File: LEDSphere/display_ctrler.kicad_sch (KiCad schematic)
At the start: 38 parts, among them J101 CONN_01x02, J301 USB_C_Receptacle_USB2.0, J302 Micro_SD_Card, U1 SN74AHC1G14DBVR, U101 W25Q128JVP, U301 USBLC6-2SC6, U303 RP2040, U305 ESP01s, Y301 12MHz

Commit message: finish display controller layout
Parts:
- J301: footprint project_lib:CUI_UJ20-C-V-C-1-SMT-TR -> Footprints:CUI_UJ20-C-V-C-1-SMT-TR
- J302: footprint project_lib:CUI_MSD-4-A -> Footprints:CUI_MSD-4-A
- U305: footprint project_lib:ESP01s_SMD -> Footprints:ESP01s_SMD
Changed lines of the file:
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@@
 			)
 		)
-		(property "Footprint" "project_lib:CUI_UJ20-C-V-C-1-SMT-TR"
+		(property "Footprint" "Footprints:CUI_UJ20-C-V-C-1-SMT-TR"
 			(at 33.02 53.34 0)
 			(hide yes)
@@
 			)
 		)
-		(property "Footprint" "project_lib:ESP01s_SMD"
+		(property "Footprint" "Footprints:ESP01s_SMD"
 			(at 246.38 71.12 0)
 			(hide yes)
@@
 			)
 		)
-		(property "Footprint" "project_lib:CUI_MSD-4-A"
+		(property "Footprint" "Footprints:CUI_MSD-4-A"
 			(at 13.97 156.21 0)
 			(show_name no)

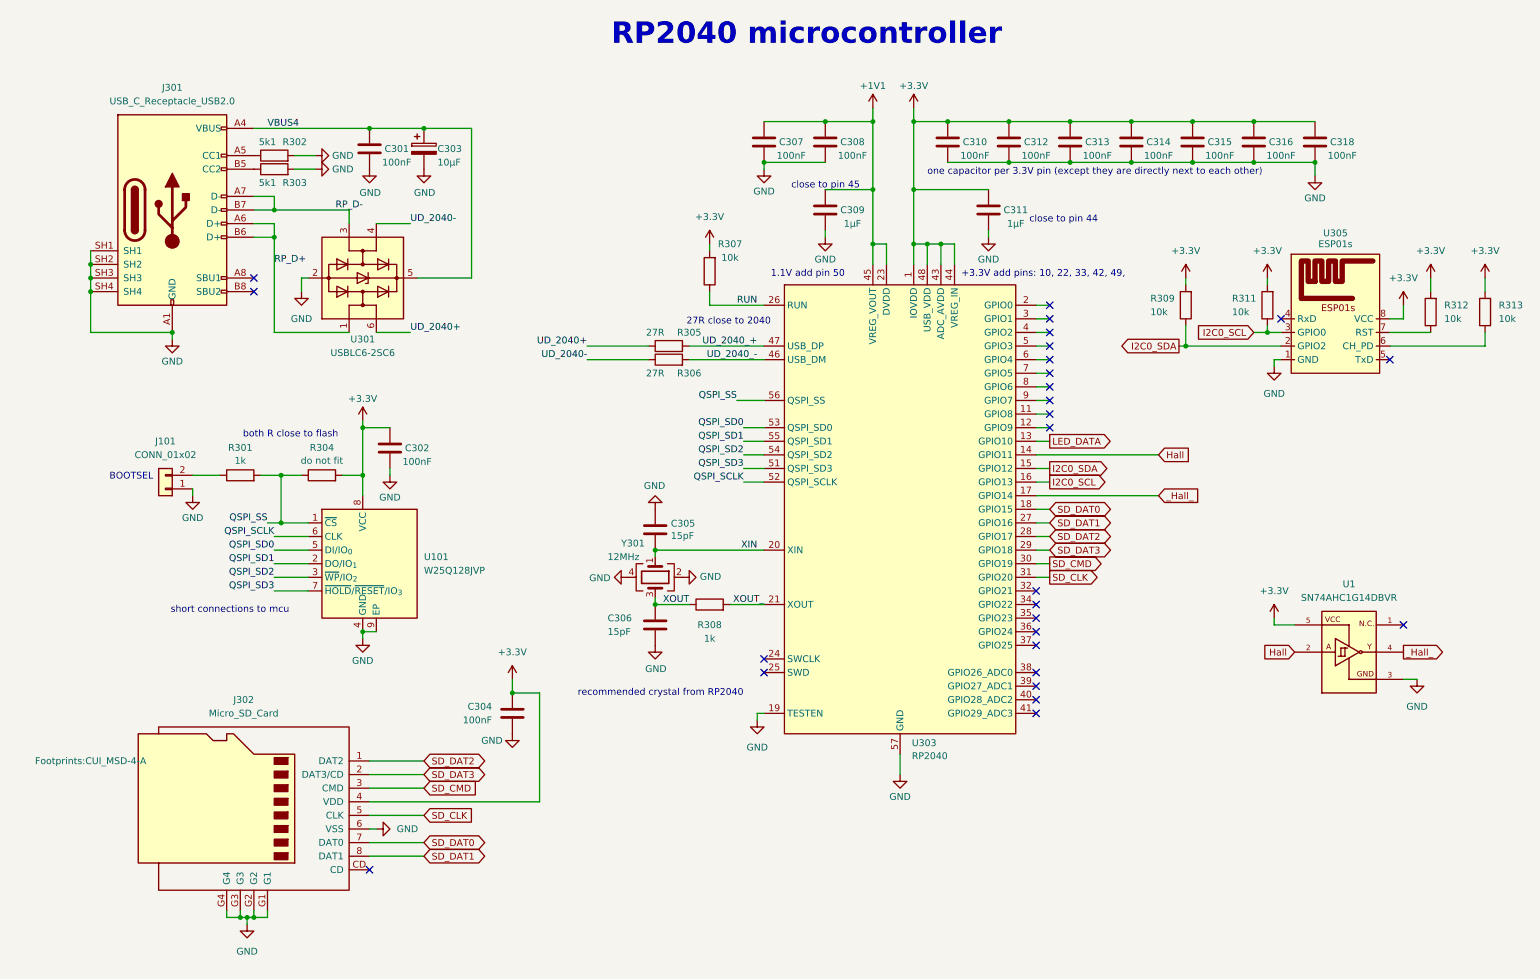
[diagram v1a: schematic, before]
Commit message: display controller add led terminal
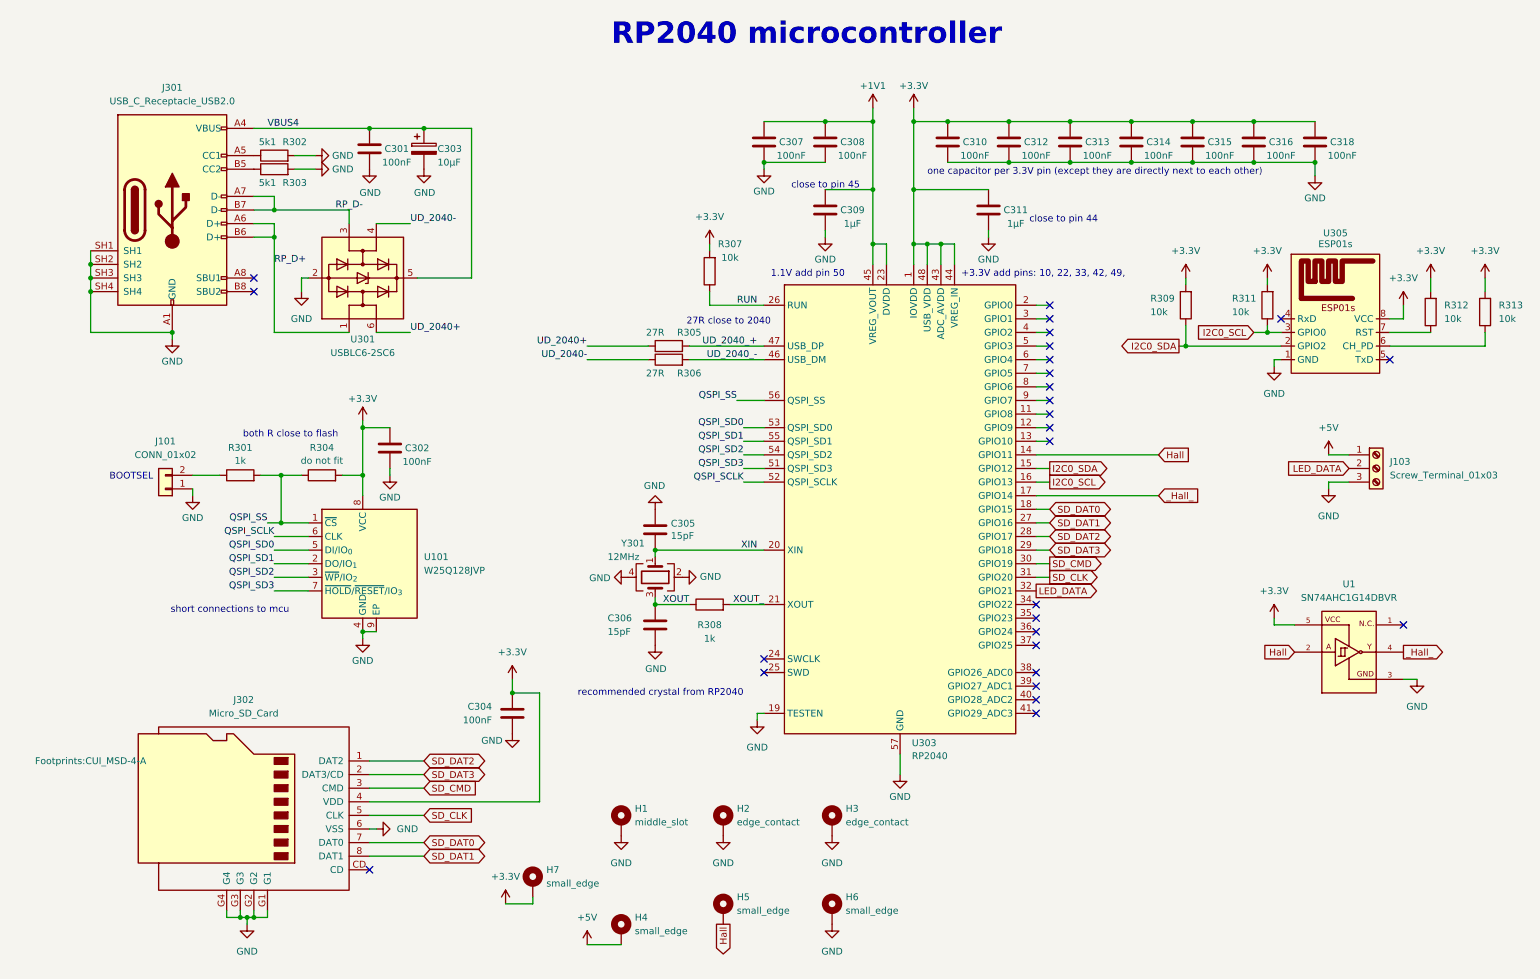
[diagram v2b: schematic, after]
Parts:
- added H1: middle_slot, Footprints:middle_slot, symbol formula:M.2_MountingHole
- added H2, H3: edge_contact, Footprints:edge_contact, symbol formula:M.2_MountingHole
- added H4, H5, H6, H7: small_edge, Footprints:edge_contact_small, symbol formula:M.2_MountingHole
- added J103: Screw_Terminal_01x03, Footprints:GCT_TAD05-03-1-L-G_REVA, symbol Connector:Screw_Terminal_01x03
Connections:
- net +3.3V: now also H7.1
- net GND: now also H1.1, H2.1, H3.1, H6.1, J103.3 (Pin_3)
- net Hall: now also H5.1
- net LED_DATA: now also U303.32 (GPIO21), J103.2 (Pin_2); no longer U303.13 (GPIO10)
- new net +5V: H4.1, J103.1 (Pin_1)

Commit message: change footprints
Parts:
- removed C303: 10µF, Capacitor_SMD:C_0805_2012Metric, symbol RD40_display_SMD-rescue:CP-Device
- removed U101: W25Q128JVP, Package_SON:WSON-8-1EP_6x5mm_P1.27mm_EP3.4x4.3mm, symbol Memory_Flash:W25Q128JVP
- added C303: 10uF, Capacitor_SMD:C_1206_3216Metric, symbol Device:C
- added U102: W25Q128JVS, Package_SO:SOIC-8_5.3x5.3mm_P1.27mm, symbol Memory_Flash:W25Q128JVS
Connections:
- net +3.3V: now also U102.8 (VCC)
- net GND: now also C303.1, U102.4 (GND)
- net QSPI_SCLK: now also U102.6 (CLK)
- net QSPI_SD0: now also U102.5 (DI/IO_{0})
- net QSPI_SD1: now also U102.2 (DO/IO_{1})
- net QSPI_SD2: now also U102.3 (~{WP}/IO_{2})
- net QSPI_SD3: now also U102.7 (~{HOLD}/~{RESET}/IO_{3})
- net QSPI_SS: now also U102.1 (~{CS})
- net VBUS4: now also C303.2
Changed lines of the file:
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@@
 	)
 	(junction
-		(at 76.2 38.1)
-		(diameter 0)
-		(color 0 0 0 0)
-	)
-	(junction
 		(at 160.02 36.83)
 		(diameter 0)
@@
 	)
 	(junction
-		(at 64.77 132.08)
-		(diameter 0)
-		(color 0 0 0 0)
-	)
-	(junction
 		(at 160.02 49.53)
 		(diameter 0)
@@
 	)
 	(junction
+		(at 76.2 38.1)
+		(diameter 0)
+		(color 0 0 0 0)
+	)
+	(junction
 		(at 196.85 44.45)
 		(diameter 0)
@@
 	(wire
 		(pts
-			(xy 76.2 38.1) (xy 85.09 38.1)
+			(xy 66.04 38.1) (xy 76.2 38.1)
 		)
 		(stroke
@@
 	(wire
 		(pts
-			(xy 64.77 132.08) (xy 67.31 132.08)
-		)
-		(stroke
-			(width 0)
-			(type default)
-		)
-	)
-	(wire
-		(pts
 			(xy 160.02 59.69) (xy 160.02 63.5)
 		)
@@
 	(wire
 		(pts
-			(xy 66.04 38.1) (xy 76.2 38.1)
-		)
-		(stroke
-			(width 0)
-			(type default)
-		)
-	)
-	(wire
-		(pts
 			(xy 44.45 184.15) (xy 44.45 185.42)
 		)
@@
 	(wire
 		(pts
+			(xy 76.2 38.1) (xy 85.09 38.1)
+		)
+		(stroke
+			(width 0)
+			(type default)
+		)
+	)
+	(wire
+		(pts
 			(xy 129.54 68.58) (xy 129.54 71.12)
 		)
@@
 	)
 	(symbol
-		(lib_id "Memory_Flash:W25Q128JVP")
-		(at 64.77 119.38 0)
-		(unit 1)
-		(body_style 1)
-		(exclude_from_sim no)
-		(in_bom yes)
-		(on_board yes)
-		(in_pos_files yes)
-		(dnp no)
-		(fields_autoplaced yes)
-		(property "Reference" "U101"
-			(at 76.2 118.1099 0)
-			(show_name no)
-			(do_not_autoplace no)
-			(effects
-				(font
-					(size 1.27 1.27)
-				)
-				(justify left)
-			)
-		)
-		(property "Value" "W25Q128JVP"
-			(at 76.2 120.6499 0)
-			(show_name no)
-			(do_not_autoplace no)
-			(effects
-				(font
-					(size 1.27 1.27)
-				)
-				(justify left)
-			)
-		)
-		(property "Footprint" "Package_SON:WSON-8-1EP_6x5mm_P1.27mm_EP3.4x4.3mm"
-			(at 64.77 96.52 0)
-			(hide yes)
-			(show_name no)
-			(do_not_autoplace no)
-			(effects
-				(font
-					(size 1.27 1.27)
-				)
-			)
-		)
-		(property "Datasheet" "https://www.winbond.com/resource-files/w25q128jv_dtr%20revc%2003272018%20plus.pdf"
-			(at 64.77 93.98 0)
-			(hide yes)
-			(show_name no)
-			(do_not_autoplace no)
-			(effects
-				(font
-					(size 1.27 1.27)
-				)
-			)
-		)
-		(property "Description" "128Mbit / 16MiB Serial Flash Memory, Standard/Dual/Quad SPI, 2.7-3.6V, WSON-8"
-			(at 64.77 91.44 0)
-			(hide yes)
-			(show_name no)
-			(do_not_autoplace no)
-			(effects
-				(font
-					(size 1.27 1.27)
-				)
-			)
-		)
-		(pin "5"
-		)
-		(pin "2"
-		)
-		(pin "9"
-		)
-		(pin "4"
-		)
-		(pin "8"
-		)
-		(pin "3"
-		)
-		(pin "7"
-		)
-		(pin "1"
-		)
-		(pin "6"
-		)
-		(instances
-			(project "display_ctrler"
-				(path "/9292a425-4deb-48f6-8b98-43cd7d592040"
-					(reference "U101")
-					(unit 1)
-				)
-			)
-		)
-	)
-	(symbol
 		(lib_id "power:+3.3V")
 		(at 64.77 92.71 0)
@@
 	)
 	(symbol
-		(lib_id "RD40_display_SMD-rescue:CP-Device")
-		(at 76.2 41.91 0)
+		(lib_id "Device:C")
+		(at 219.71 40.64 180)
 		(unit 1)
 		(body_style 1)
@@
 		(in_pos_files yes)
 		(dnp no)
-		(property "Reference" "C303"
-			(at 78.74 41.91 0)
+		(property "Reference" "C315"
+			(at 224.79 40.64 0)
 			(show_name no)
 			(do_not_autoplace no)
@@
 					(size 1.27 1.27)
 				)
-				(justify left)
 			)
 		)
-		(property "Value" "10µF"
-			(at 78.74 44.45 0)
+		(property "Value" "100nF"
+			(at 224.79 43.18 0)
 			(show_name no)
 			(do_not_autoplace no)
@@
 					(size 1.27 1.27)
 				)
-				(justify left)
 			)
 		)
-		(property "Footprint" "Capacitor_SMD:C_0805_2012Metric"
-			(at 77.1652 45.72 0)
+		(property "Footprint" "Capacitor_SMD:C_0603_1608Metric"
+			(at 218.7448 36.83 0)
 			(hide yes)
 			(show_name no)
@@
 		)
 		(property "Datasheet" ""
-			(at 76.2 41.91 0)
+			(at 219.71 40.64 0)
 			(hide yes)
 			(show_name no)
@@
 		)
 		(property "Description" ""
-			(at 76.2 41.91 0)
+			(at 219.71 40.64 0)
 			(hide yes)
 			(show_name no)
@@
 			)
 		)
-		(property "LCSC" "C15850"
-			(at 76.2 41.91 0)
+		(property "LCSC" "C307331"
+			(at 219.71 40.64 0)
 			(hide yes)
 			(show_name no)
@@
 			(project "display_ctrler"
 				(path "/9292a425-4deb-48f6-8b98-43cd7d592040"
-					(reference "C303")
+					(reference "C315")
 					(unit 1)
 				)
@@
 	)
 	(symbol
-		(lib_id "Device:C")
-		(at 219.71 40.64 180)
+		(lib_id "Device:R")
+		(at 121.92 78.74 90)
 		(unit 1)
 		(body_style 1)
@@
 		(in_pos_files yes)
 		(dnp no)
-		(property "Reference" "C315"
-			(at 224.79 40.64 0)
+		(property "Reference" "R305"
+			(at 125.73 76.2 90)
 			(show_name no)
 			(do_not_autoplace no)
@@
 			)
 		)
-		(property "Value" "100nF"
-			(at 224.79 43.18 0)
+		(property "Value" "27R"
+			(at 119.38 76.2 90)
 			(show_name no)
 			(do_not_autoplace no)
@@
 			)
 		)
-		(property "Footprint" "Capacitor_SMD:C_0603_1608Metric"
-			(at 218.7448 36.83 0)
+		(property "Footprint" "Resistor_SMD:R_0603_1608Metric"
+			(at 121.92 80.518 90)
 			(hide yes)
 			(show_name no)
@@
 		)
 		(property "Datasheet" ""
-			(at 219.71 40.64 0)
+			(at 121.92 78.74 0)
 			(hide yes)
 			(show_name no)
@@
 		)
 		(property "Description" ""
-			(at 219.71 40.64 0)
+			(at 121.92 78.74 0)
 			(hide yes)
 			(show_name no)
@@
 			)
 		)
-		(property "LCSC" "C307331"
-			(at 219.71 40.64 0)
+		(property "LCSC" "C321419"
+			(at 121.92 78.74 90)
 			(hide yes)
 			(show_name no)
@@
 			(project "display_ctrler"
 				(path "/9292a425-4deb-48f6-8b98-43cd7d592040"
-					(reference "C315")
+					(reference "R305")
 					(unit 1)
 				)
@@
 	)
 	(symbol
-		(lib_id "Device:R")
-		(at 121.92 78.74 90)
+		(lib_id "Device:C")
+		(at 76.2 41.91 180)
 		(unit 1)
 		(body_style 1)
@@
 		(in_pos_files yes)
 		(dnp no)
-		(property "Reference" "R305"
-			(at 125.73 76.2 90)
+		(property "Reference" "C303"
+			(at 81.28 41.91 0)
 			(show_name no)
 			(do_not_autoplace no)
@@
 			)
 		)
-		(property "Value" "27R"
-			(at 119.38 76.2 90)
+		(property "Value" "10uF"
+			(at 81.28 44.45 0)
 			(show_name no)
 			(do_not_autoplace no)
@@
 			)
 		)
-		(property "Footprint" "Resistor_SMD:R_0603_1608Metric"
-			(at 121.92 80.518 90)
+		(property "Footprint" "Capacitor_SMD:C_1206_3216Metric"
+			(at 75.2348 38.1 0)
 			(hide yes)
 			(show_name no)
@@
 		)
 		(property "Datasheet" ""
-			(at 121.92 78.74 0)
+			(at 76.2 41.91 0)
 			(hide yes)
 			(show_name no)
@@
 		)
 		(property "Description" ""
-			(at 121.92 78.74 0)
+			(at 76.2 41.91 0)
 			(hide yes)
 			(show_name no)
@@
 			)
 		)
-		(property "LCSC" "C321419"
-			(at 121.92 78.74 90)
+		(property "LCSC" "C307331"
+			(at 76.2 41.91 0)
 			(hide yes)
 			(show_name no)
@@
 			(project "display_ctrler"
 				(path "/9292a425-4deb-48f6-8b98-43cd7d592040"
-					(reference "R305")
+					(reference "C303")
 					(unit 1)
 				)
@@
 					(unit 1)
 				)
+			)
+		)
+	)
+	(symbol
+		(lib_id "Memory_Flash:W25Q128JVS")
+		(at 64.77 119.38 0)
+		(unit 1)
+		(body_style 1)
+		(exclude_from_sim no)
+		(in_bom yes)
+		(on_board yes)
+		(in_pos_files yes)
+		(dnp no)
+		(fields_autoplaced yes)
+		(property "Reference" "U102"
+			(at 76.2 118.1099 0)
+			(show_name no)
+			(do_not_autoplace no)
+			(effects
+				(font
+					(size 1.27 1.27)
+				)
+				(justify left)
+			)
+		)
+		(property "Value" "W25Q128JVS"
+			(at 76.2 120.6499 0)
+			(show_name no)
+			(do_not_autoplace no)
+			(effects
+				(font
+					(size 1.27 1.27)
+				)
+				(justify left)
+			)
+		)
+		(property "Footprint" "Package_SO:SOIC-8_5.3x5.3mm_P1.27mm"
+			(at 64.77 96.52 0)
+			(hide yes)
+			(show_name no)
+			(do_not_autoplace no)
+			(effects
+				(font
+					(size 1.27 1.27)
+				)
+			)
+		)
+		(property "Datasheet" "https://www.winbond.com/resource-files/w25q128jv_dtr%20revc%2003272018%20plus.pdf"
+			(at 64.77 93.98 0)
+			(hide yes)
+			(show_name no)
+			(do_not_autoplace no)
+			(effects
+				(font
+					(size 1.27 1.27)
+				)
+			)
+		)
+		(property "Description" "128Mbit / 16MiB Serial Flash Memory, Standard/Dual/Quad SPI, 2.7-3.6V, SOIC-8"
+			(at 64.77 91.44 0)
+			(hide yes)
+			(show_name no)
+			(do_not_autoplace no)
+			(effects
+				(font
+					(size 1.27 1.27)
+				)
+			)
+		)
+		(pin "3"
+		)
+		(pin "4"
+		)
+		(pin "2"
+		)
+		(pin "5"
+		)
+		(pin "6"
+		)
+		(pin "8"
+		)
+		(pin "7"
+		)
+		(pin "1"
+		)
+		(instances
+			(project "display_ctrler"
+				(path "/9292a425-4deb-48f6-8b98-43cd7d592040"
+					(reference "U102")
+					(unit 1)
+				)

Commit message: display ctrler changes
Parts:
- R302, R303: value 5k1 -> 5.1k
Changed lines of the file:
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@@
 			)
 		)
-		(property "Value" "5k1"
+		(property "Value" "5.1k"
 			(at 46.99 48.26 90)
 			(show_name no)
@@
 			)
 		)
-		(property "Value" "5k1"
+		(property "Value" "5.1k"
 			(at 46.99 40.64 90)
 			(show_name no)

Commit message: FINAL PUSHES
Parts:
- added D1, D2: LED, LED_SMD:LED_0805_2012Metric, symbol Device:LED
- added R310, R314: 1k, Resistor_SMD:R_0603_1608Metric, symbol Device:R
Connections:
- net +3.3V: now also D1.2 (A)
- net +5V: now also D2.2 (A)
- net GND: now also R310.1, R314.1
- new net: D2.1 (K), R314.2
- new net: D1.1 (K), R310.2
